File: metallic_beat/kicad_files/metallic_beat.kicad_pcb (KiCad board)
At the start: 2 copper layers, 68.6 x 50 mm, 66 parts, among them J1 GATE_IN, J2 AUDIO_OUT, J3 POWER, Q1 BC337, Q2 BC547, Q3 BC547, Q4 BC337, U1 4069

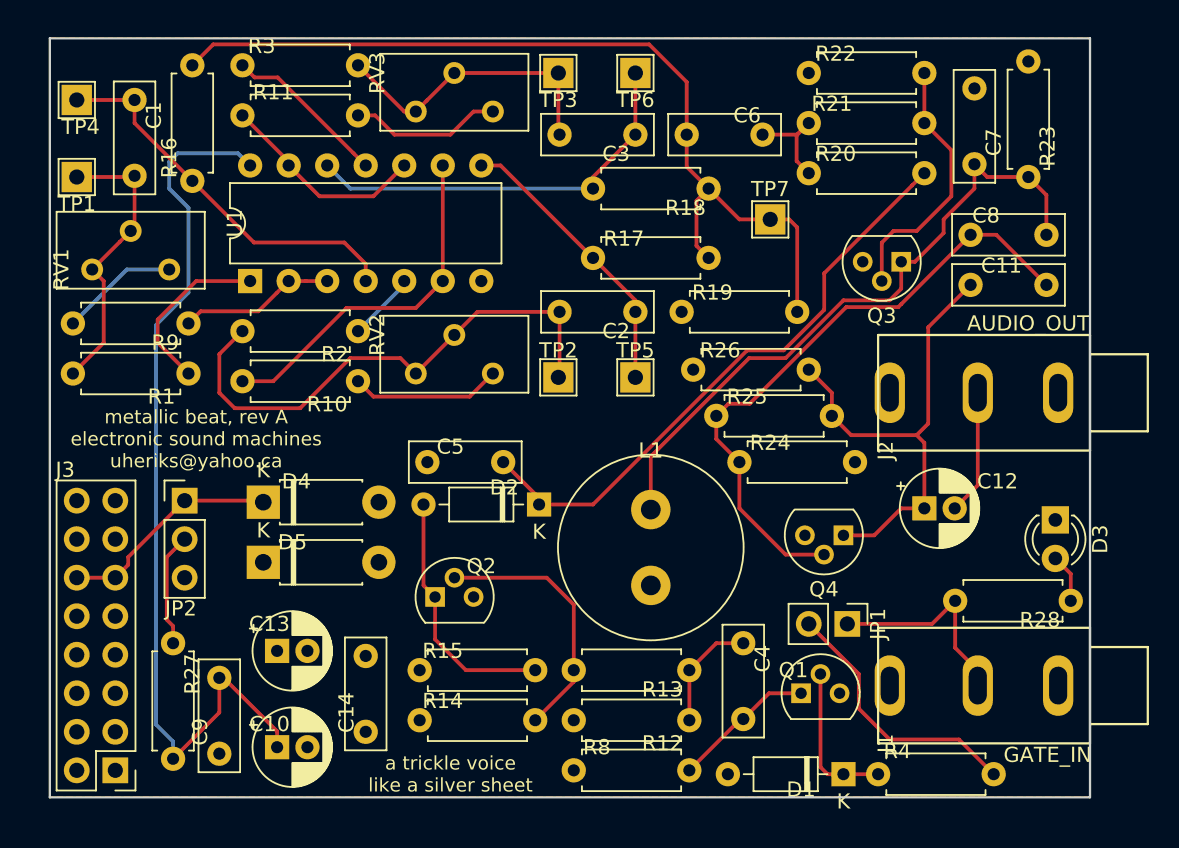
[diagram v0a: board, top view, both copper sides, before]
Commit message: metallic beat: Add jumper for VCA
Mainly for test and experimentation purposes, having a jumper in
the oscillator signal's path to the VCA/filter thing could be nice
to make it possible to run other things through there.

NOTE: When building,one will have to add a capacitor on the jack!
I figured the existing one would be too small to use as a
decoupling capacitor.
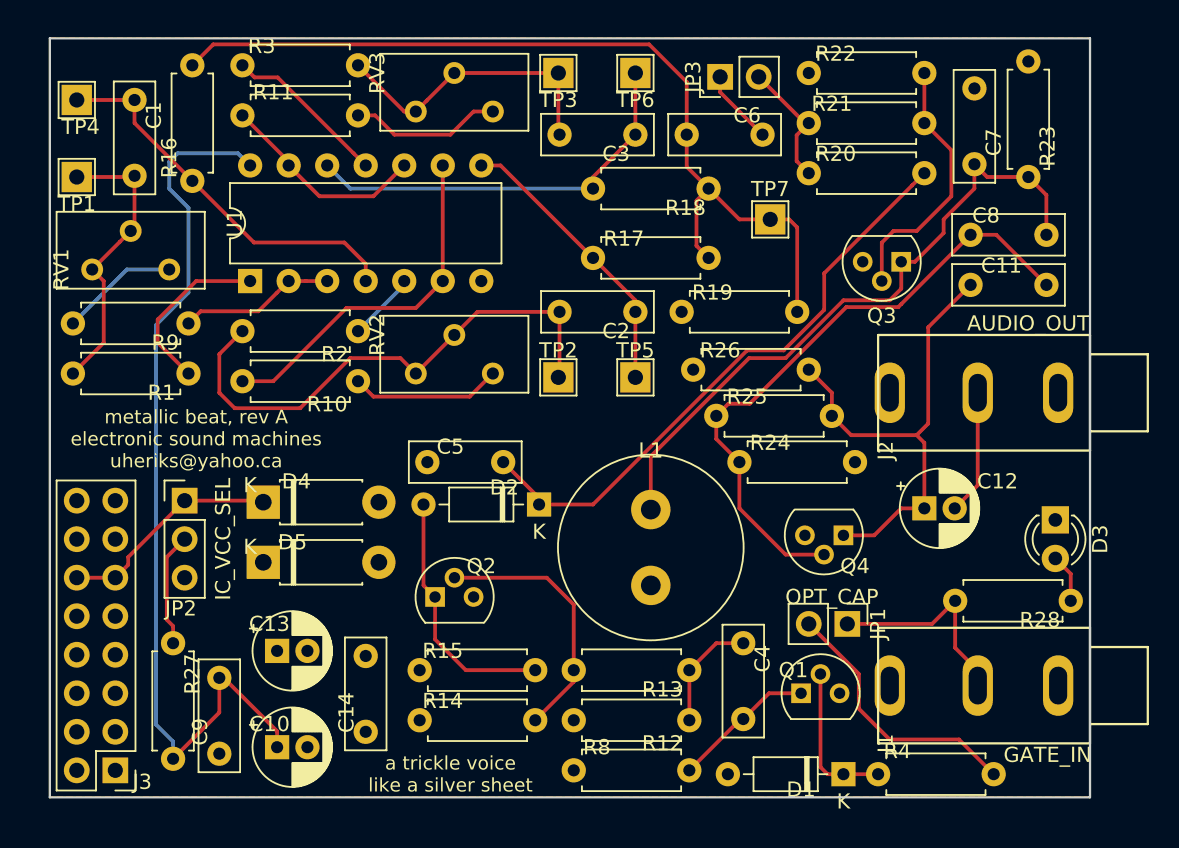
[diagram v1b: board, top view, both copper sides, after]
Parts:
- added JP3: VCA_IN, Connector_PinHeader_2.54mm:PinHeader_1x02_P2.54mm_Vertical, F.Cu at (153.4, 64.3)
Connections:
- R20 pad 1: Net-(C6-Pad1) -> Net-(JP3-Pad2)
- R21 pad 2: Net-(C6-Pad1) -> Net-(JP3-Pad2)
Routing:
- net Net-(JP3-Pad2): track 0.00 -> 8.53 mm
- net Net-(C6-Pad1): track 7.33 -> 4.97 mm
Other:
- board text added: "IC_VCC_SEL"
- board text added: "OPT_CAP"
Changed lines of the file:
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@@
   (general
     (thickness 1.6)
-    (drawings 18)
-    (tracks 218)
+    (drawings 20)
+    (tracks 220)
     (zones 0)
-    (modules 66)
-    (nets 37)
+    (modules 67)
+    (nets 38)
   )
   (page A4)
@@
   (net 35 "Net-(Q2-Pad2)")
   (net 36 "Net-(Q3-Pad2)")
+  (net 37 "Net-(JP3-Pad2)")
   (net_class Default "This is the default net class."
     (clearance 0.2)
@@
     (add_net "Net-(JP1-Pad2)")
     (add_net "Net-(JP2-Pad2)")
+    (add_net "Net-(JP3-Pad2)")
     (add_net "Net-(Q2-Pad2)")
     (add_net "Net-(Q3-Pad2)")
@@
     (descr "Through hole straight pin header, 2x08, 2.54mm pitch, double rows")
     (tags "Through hole pin header THT 2x08 2.54mm double row")
-    (fp_text reference J3 (at 3.302 19.812 180) (layer F.SilkS)
+    (fp_text reference J3 (at -1.778 -0.762 180) (layer F.SilkS)
       (effects (font (size 1 1) (thickness 0.15)))
     )
@@
       (effects (font (size 1 1) (thickness 0.15)))
     )
-    (fp_text value OPT_CAP (at 0 4.87 270) (layer F.Fab)
+    (fp_text value OPT_CAP (at -1.778 1.016) (layer F.Fab)
       (effects (font (size 1 1) (thickness 0.15)))
     )
@@
     (descr "Resistor, Axial_DIN0207 series, Axial, Horizontal, pin pitch=7.62mm, 0.25W = 1/4W, length*diameter=6.3*2.5mm^2, http://cdn-reichelt.de/documents/datenblatt/B400/1_4W%23YAG.pdf")
     (tags "Resistor Axial_DIN0207 series Axial Horizontal pin pitch 7.62mm 0.25W = 1/4W length 6.3mm diameter 2.5mm")
-    (fp_text reference R1 (at 1.778 -1.524 180) (layer F.SilkS)
+    (fp_text reference R1 (at 1.778 -1.27 180) (layer F.SilkS)
       (effects (font (size 1 1) (thickness 0.15)))
     )
@@
       (effects (font (size 1 1) (thickness 0.15)))
     )
-    (fp_text user %R (at 1.778 -1.524 180) (layer F.Fab)
+    (fp_text user %R (at 1.778 -1.27 180) (layer F.Fab)
       (effects (font (size 1 1) (thickness 0.15)))
     )
@@
       (net 9 "Net-(C5-Pad2)"))
     (pad 1 thru_hole circle (at 0 0) (size 1.6 1.6) (drill 0.8) (layers *.Cu *.Mask)
-      (net 11 "Net-(C6-Pad1)"))
+      (net 37 "Net-(JP3-Pad2)"))
     (model ${KISYS3DMOD}/Resistor_THT.3dshapes/R_Axial_DIN0207_L6.3mm_D2.5mm_P7.62mm_Horizontal.wrl
       (at (xyz 0 0 0))
@@
     (fp_line (start 0.66 -1.25) (end 0.66 1.25) (layer F.Fab) (width 0.1))
     (pad 2 thru_hole oval (at 7.62 0 180) (size 1.6 1.6) (drill 0.8) (layers *.Cu *.Mask)
-      (net 11 "Net-(C6-Pad1)"))
+      (net 37 "Net-(JP3-Pad2)"))
     (pad 1 thru_hole circle (at 0 0 180) (size 1.6 1.6) (drill 0.8) (layers *.Cu *.Mask)
       (net 36 "Net-(Q3-Pad2)"))
@@
     (descr "TO-92L leads in-line (large body variant of TO-92), also known as TO-226, wide, drill 0.75mm (see https://www.diodes.com/assets/Package-Files/TO92L.pdf and http://www.ti.com/lit/an/snoa059/snoa059.pdf)")
     (tags "TO-92L Molded Narrow transistor")
-    (fp_text reference Q4 (at 1.29 -3.56 180) (layer F.SilkS)
+    (fp_text reference Q4 (at -0.762 -2.032 180) (layer F.SilkS)
       (effects (font (size 1 1) (thickness 0.15)))
     )
@@
       (effects (font (size 1 1) (thickness 0.15)))
     )
-    (fp_text user %R (at 1.29 -3.56 180) (layer F.Fab)
+    (fp_text user %R (at -0.762 -2.032 180) (layer F.Fab)
       (effects (font (size 1 1) (thickness 0.15)))
     )
@@
       (effects (font (size 1 1) (thickness 0.15)))
     )
-    (fp_text user K (at 0 -2.1) (layer F.Fab)
+    (fp_text user K (at -0.867001 -1.117001) (layer F.Fab)
       (effects (font (size 1 1) (thickness 0.15)))
     )
-    (fp_text user K (at 0 -2.1) (layer F.SilkS)
+    (fp_text user K (at -0.867001 -1.117001) (layer F.SilkS)
       (effects (font (size 1 1) (thickness 0.15)))
     )
@@
       (effects (font (size 1 1) (thickness 0.15)))
     )
-    (fp_text user K (at 0 -2.1) (layer F.SilkS)
+    (fp_text user K (at -0.867001 -1.016) (layer F.SilkS)
       (effects (font (size 1 1) (thickness 0.15)))
     )
-    (fp_text user K (at 0 -2.1) (layer F.Fab)
+    (fp_text user K (at -0.867001 -1.016) (layer F.Fab)
       (effects (font (size 1 1) (thickness 0.15)))
     )
@@
       (xy -16.848667 -8.580966)) (layer Eco2.User) (width 0.01))
   )
+  (module Connector_PinHeader_2.54mm:PinHeader_1x02_P2.54mm_Vertical (layer F.Cu)
+    (at 153.416 64.262 90)
+    (descr "Through hole straight pin header, 1x02, 2.54mm pitch, single row")
+    (tags "Through hole pin header THT 1x02 2.54mm single row")
+    (fp_text reference JP3 (at 0 -1.778 90) (layer F.SilkS)
+      (effects (font (size 1 1) (thickness 0.15)))
+    )
+    (fp_text value VCA_IN (at 1.778 1.27 180) (layer F.Fab)
+      (effects (font (size 1 1) (thickness 0.15)))
+    )
+    (fp_line (start -0.635 -1.27) (end 1.27 -1.27) (layer F.Fab) (width 0.1))
+    (fp_line (start 1.27 -1.27) (end 1.27 3.81) (layer F.Fab) (width 0.1))
+    (fp_line (start 1.27 3.81) (end -1.27 3.81) (layer F.Fab) (width 0.1))
+    (fp_line (start -1.27 3.81) (end -1.27 -0.635) (layer F.Fab) (width 0.1))
+    (fp_line (start -1.27 -0.635) (end -0.635 -1.27) (layer F.Fab) (width 0.1))
+    (fp_line (start -1.33 3.87) (end 1.33 3.87) (layer F.SilkS) (width 0.12))
+    (fp_line (start -1.33 1.27) (end -1.33 3.87) (layer F.SilkS) (width 0.12))
+    (fp_line (start 1.33 1.27) (end 1.33 3.87) (layer F.SilkS) (width 0.12))
+    (fp_line (start -1.33 1.27) (end 1.33 1.27) (layer F.SilkS) (width 0.12))
+    (fp_line (start -1.33 0) (end -1.33 -1.33) (layer F.SilkS) (width 0.12))
+    (fp_line (start -1.33 -1.33) (end 0 -1.33) (layer F.SilkS) (width 0.12))
+    (fp_line (start -1.8 -1.8) (end -1.8 4.35) (layer F.CrtYd) (width 0.05))
+    (fp_line (start -1.8 4.35) (end 1.8 4.35) (layer F.CrtYd) (width 0.05))
+    (fp_line (start 1.8 4.35) (end 1.8 -1.8) (layer F.CrtYd) (width 0.05))
+    (fp_line (start 1.8 -1.8) (end -1.8 -1.8) (layer F.CrtYd) (width 0.05))
+    (fp_text user %R (at 0 1.27 180) (layer F.Fab)
+      (effects (font (size 1 1) (thickness 0.15)))
+    )
+    (pad 1 thru_hole rect (at 0 0 90) (size 1.7 1.7) (drill 1) (layers *.Cu *.Mask)
+      (net 11 "Net-(C6-Pad1)"))
+    (pad 2 thru_hole oval (at 0 2.54 90) (size 1.7 1.7) (drill 1) (layers *.Cu *.Mask)
+      (net 37 "Net-(JP3-Pad2)"))
+    (model ${KISYS3DMOD}/Connector_PinHeader_2.54mm.3dshapes/PinHeader_1x02_P2.54mm_Vertical.wrl
+      (at (xyz 0 0 0))
+      (scale (xyz 1 1 1))
+      (rotate (xyz 0 0 0))
+    )
+  )
+  (gr_text IC_VCC_SEL (at 120.65 94.742 90) (layer F.SilkS)
+    (effects (font (size 1 1) (thickness 0.2)))
+  )
+  (gr_text OPT_CAP (at 160.782 98.552) (layer F.SilkS)
+    (effects (font (size 1 1) (thickness 0.2)))
+  )
   (gr_text "Prototype note: Also, the trim pots could naturally be replaced with panel \npotentiometers, for extra tweakability (untested, so not sure if it’s useful)." (at 108.712 146.812) (layer Cmts.User)
     (effects (font (size 1.3 1.3) (thickness 0.2)) (justify left))
@@
   (segment (start 160.274 77.216) (end 166.078001 71.411999) (width 0.25) (layer F.Cu) (net 9))
   (segment (start 166.078001 71.411999) (end 166.878 70.612) (width 0.25) (layer F.Cu) (net 9))
-  (segment (start 158.496 68.072) (end 159.258 67.31) (width 0.25) (layer F.Cu) (net 11))
-  (segment (start 156.21 68.072) (end 158.496 68.072) (width 0.25) (layer F.Cu) (net 11))
-  (segment (start 158.458001 69.812001) (end 159.258 70.612) (width 0.25) (layer F.Cu) (net 11))
-  (segment (start 158.458001 68.109999) (end 158.458001 69.812001) (width 0.25) (layer F.Cu) (net 11))
-  (segment (start 159.258 67.31) (end 158.458001 68.109999) (width 0.25) (layer F.Cu) (net 11))
+  (segment (start 153.416 65.278) (end 153.416 64.262) (width 0.25) (layer F.Cu) (net 11))
+  (segment (start 156.21 68.072) (end 153.416 65.278) (width 0.25) (layer F.Cu) (net 11))
+  (segment (start 158.458001 69.812001) (end 159.258 70.612) (width 0.25) (layer F.Cu) (net 37))
+  (segment (start 158.458001 68.109999) (end 158.458001 69.812001) (width 0.25) (layer F.Cu) (net 37))
+  (segment (start 159.258 67.31) (end 158.458001 68.109999) (width 0.25) (layer F.Cu) (net 37))
   (segment (start 119.99599 62.12201) (end 148.73601 62.12201) (width 0.25) (layer F.Cu) (net 12))
   (segment (start 118.618 63.5) (end 119.99599 62.12201) (width 0.25) (layer F.Cu) (net 12))
@@
   (segment (start 168.656 69.088) (end 166.878 67.31) (width 0.25) (layer F.Cu) (net 36))
   (segment (start 168.656 72.136) (end 168.656 69.088) (width 0.25) (layer F.Cu) (net 36))
+  (segment (start 159.004 67.31) (end 159.258 67.31) (width 0.25) (layer F.Cu) (net 37))
+  (segment (start 155.956 64.262) (end 159.004 67.31) (width 0.25) (layer F.Cu) (net 37))
   (zone (net 10) (net_name GND) (layer B.Cu) (hatch edge 0.508)
     (connect_pads (clearance 0.508))
